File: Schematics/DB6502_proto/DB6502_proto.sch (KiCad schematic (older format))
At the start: 28 parts, among them SW1 Reset, U1 DS1813, U10 62256, U11 74AC138, U12 28C256, U13 22V10C, U2 74AC32, U3 74HC21, U4 65C02S, U5 74AC74, U6 74HC74, U7 74AC04, U8 62256, U9 74AC08, X1 14MHz

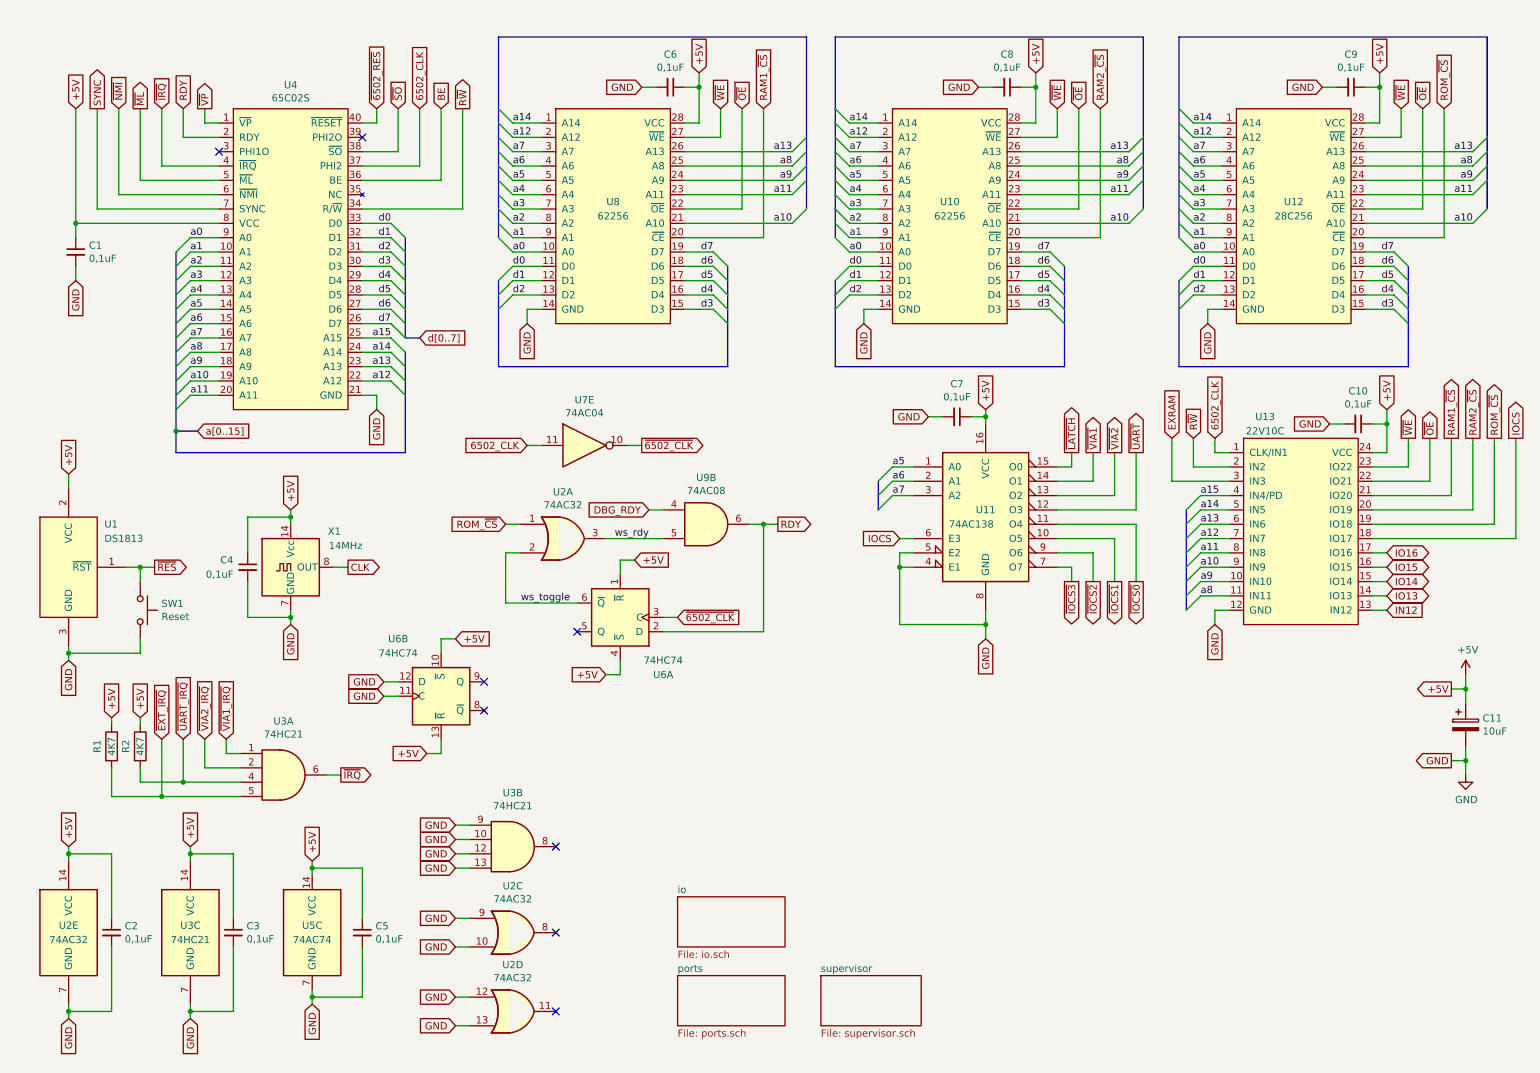
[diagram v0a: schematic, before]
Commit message: Added second USB channel to UART
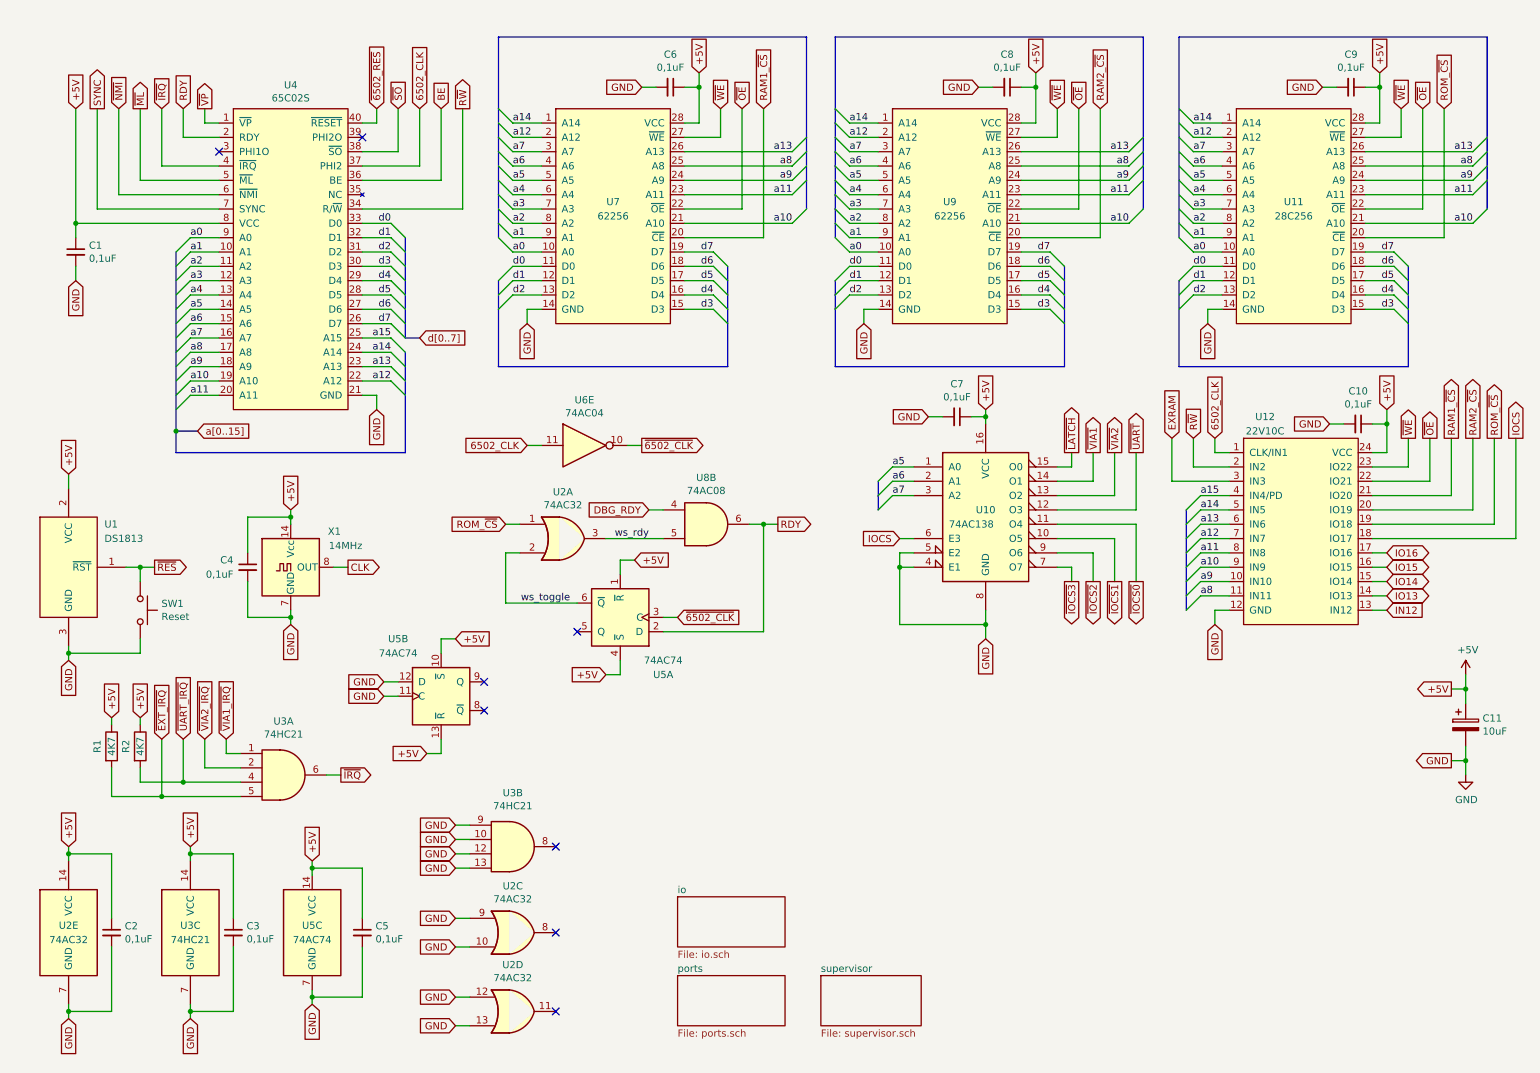
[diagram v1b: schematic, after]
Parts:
- C1, C10, C2, C3, C4, C5, C6, C7, C8, C9: footprint (none) -> Capacitor_THT:C_Disc_D5.0mm_W2.5mm_P2.50mm
- R1, R2: footprint (none) -> Resistor_THT:R_Axial_DIN0207_L6.3mm_D2.5mm_P10.16mm_Horizontal
- U2, U5: footprint (none) -> Package_DIP:DIP-14_W7.62mm_Socket
- U3: footprint (none) -> Package_DIP:DIP-12_W7.62mm_Socket
- U5: renamed from U6; value 74HC74 -> 74AC74; footprint (none) -> Package_DIP:DIP-14_W7.62mm_Socket
- U6: renamed from U7; footprint (none) -> Package_DIP:DIP-14_W7.62mm_Socket
- U8: renamed from U9; footprint (none) -> Package_DIP:DIP-14_W7.62mm_Socket
- renumbered U11 to U10, U12 to U11, U13 to U12, U8 to U7, U10 to U9
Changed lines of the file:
@@
 	10600 5200 10600 5300
 $Comp
-L 6502:22V10C U13
+L 6502:22V10C U12
 U 1 1 5F680A6E
 P 9450 4100
-F 0 "U13" H 9200 4900 50  0000 C CNN
+F 0 "U12" H 9200 4900 50  0000 C CNN
 F 1 "22V10C" H 9200 4800 50  0000 C CNN
 F 2 "Package_DIP:DIP-24_W7.62mm_Socket" H 9450 3400 50  0001 C CNN
@@
 Connection ~ 1350 4350
 $Comp
-L 74xx:74LS138 U11
+L 74xx:74LS138 U10
 U 1 1 5F9A1F2C
 P 7250 3950
-F 0 "U11" H 7250 3950 50  0000 C CNN
+F 0 "U10" H 7250 3950 50  0000 C CNN
 F 1 "74AC138" H 7150 3850 50  0000 C CNN
 F 2 "Package_DIP:DIP-16_W7.62mm_Socket" H 7250 3950 50  0001 C CNN
@@
 $EndComp
 $Comp
-L 6502:62256 U10
+L 6502:62256 U9
 U 1 1 5F5FD943
 P 7000 1900
-F 0 "U10" H 7000 2000 50  0000 C CNN
+F 0 "U9" H 7000 2000 50  0000 C CNN
 F 1 "62256" H 7000 1900 50  0000 C CNN
 F 2 "Package_DIP:DIP-28_W15.24mm_Socket" H 6950 2700 50  0001 C CNN
@@
 $EndComp
 $Comp
-L 6502:62256 U8
+L 6502:62256 U7
 U 1 1 5F5BE432
 P 4650 1900
-F 0 "U8" H 4650 2000 50  0000 C CNN
+F 0 "U7" H 4650 2000 50  0000 C CNN
 F 1 "62256" H 4650 1900 50  0000 C CNN
 F 2 "Package_DIP:DIP-28_W15.24mm_Socket" H 4600 2700 50  0001 C CNN
@@
 $EndComp
 $Comp
-L 6502:28C256 U12
+L 6502:28C256 U11
 U 1 1 5F605CEF
 P 9400 1900
-F 0 "U12" H 9400 2000 50  0000 C CNN
+F 0 "U11" H 9400 2000 50  0000 C CNN
 F 1 "28C256" H 9400 1900 50  0000 C CNN
 F 2 "Package_DIP:DIP-28_W15.24mm_Socket" H 9350 2700 50  0001 C CNN
@@
 P 4450 3500
 AR Path="/5F8F4E1E/5FD6D1DD" Ref="U?"  Part="5"
-AR Path="/5FD6D1DD" Ref="U7"  Part="5"
-F 0 "U7" H 4450 3817 50  0000 C CNN
+AR Path="/5FD6D1DD" Ref="U6"  Part="5"
+F 0 "U6" H 4450 3817 50  0000 C CNN
 F 1 "74AC04" H 4450 3726 50  0000 C CNN
-F 2 "" H 4450 3500 50  0001 C CNN
+F 2 "Package_DIP:DIP-14_W7.62mm_Socket" H 4450 3500 50  0001 C CNN
 F 3 "https://www.ti.com/lit/ds/symlink/sn74ac04.pdf" H 4450 3500 50  0001 C CNN
 	5    4450 3500
@@
 P 5300 4050
 AR Path="/5F8F4E1E/5FDA6F78" Ref="U?"  Part="2"
-AR Path="/5FDA6F78" Ref="U9"  Part="2"
-F 0 "U9" H 5300 4375 50  0000 C CNN
+AR Path="/5FDA6F78" Ref="U8"  Part="2"
+F 0 "U8" H 5300 4375 50  0000 C CNN
 F 1 "74AC08" H 5300 4284 50  0000 C CNN
-F 2 "" H 5300 4050 50  0001 C CNN
+F 2 "Package_DIP:DIP-14_W7.62mm_Socket" H 5300 4050 50  0001 C CNN
 F 3 "https://www.ti.com/lit/ds/symlink/sn74ac08.pdf" H 5300 4050 50  0001 C CNN
 	2    5300 4050
@@
 F 0 "U2" H 4300 4475 50  0000 C CNN
 F 1 "74AC32" H 4300 4384 50  0000 C CNN
-F 2 "" H 4300 4150 50  0001 C CNN
+F 2 "Package_DIP:DIP-14_W7.62mm_Socket" H 4300 4150 50  0001 C CNN
 F 3 "http://www.ti.com/lit/gpn/sn74LS32" H 4300 4150 50  0001 C CNN
 	1    4300 4150
@@
 P 4700 4700
 AR Path="/5F8F4E1E/5FE3D22B" Ref="U?"  Part="2"
-AR Path="/5FE3D22B" Ref="U6"  Part="1"
-F 0 "U6" H 4400 5100 50  0000 C CNN
-F 1 "74HC74" H 4400 5000 50  0000 C CNN
-F 2 "" H 4700 4700 50  0001 C CNN
+AR Path="/5FE3D22B" Ref="U5"  Part="1"
+F 0 "U5" H 4400 5100 50  0000 C CNN
+F 1 "74AC74" H 4400 5000 50  0000 C CNN
+F 2 "Package_DIP:DIP-14_W7.62mm_Socket" H 4700 4700 50  0001 C CNN
 F 3 "74xx/74hc_hct74.pdf" H 4700 4700 50  0001 C CNN
 	1    4700 4700
@@
 F 0 "C1" H 992 2196 50  0000 L CNN
 F 1 "0,1uF" H 992 2105 50  0000 L CNN
-F 2 "" H 900 2150 50  0001 C CNN
+F 2 "Capacitor_THT:C_Disc_D5.0mm_W2.5mm_P2.50mm" H 900 2150 50  0001 C CNN
 F 3 "~" H 900 2150 50  0001 C CNN
 	1    900  2150
@@
 F 0 "C6" V 4821 1000 50  0000 C CNN
 F 1 "0,1uF" V 4912 1000 50  0000 C CNN
-F 2 "" H 5050 1000 50  0001 C CNN
+F 2 "Capacitor_THT:C_Disc_D5.0mm_W2.5mm_P2.50mm" H 5050 1000 50  0001 C CNN
 F 3 "~" H 5050 1000 50  0001 C CNN
 	1    5050 1000
@@
 F 0 "C8" V 7171 1000 50  0000 C CNN
 F 1 "0,1uF" V 7262 1000 50  0000 C CNN
-F 2 "" H 7400 1000 50  0001 C CNN
+F 2 "Capacitor_THT:C_Disc_D5.0mm_W2.5mm_P2.50mm" H 7400 1000 50  0001 C CNN
 F 3 "~" H 7400 1000 50  0001 C CNN
 	1    7400 1000
@@
 F 0 "C9" V 9571 1000 50  0000 C CNN
 F 1 "0,1uF" V 9662 1000 50  0000 C CNN
-F 2 "" H 9800 1000 50  0001 C CNN
+F 2 "Capacitor_THT:C_Disc_D5.0mm_W2.5mm_P2.50mm" H 9800 1000 50  0001 C CNN
 F 3 "~" H 9800 1000 50  0001 C CNN
 	1    9800 1000
@@
 F 0 "C10" V 9621 3350 50  0000 C CNN
 F 1 "0,1uF" V 9712 3350 50  0000 C CNN
-F 2 "" H 9850 3350 50  0001 C CNN
+F 2 "Capacitor_THT:C_Disc_D5.0mm_W2.5mm_P2.50mm" H 9850 3350 50  0001 C CNN
 F 3 "~" H 9850 3350 50  0001 C CNN
 	1    9850 3350
@@
 F 0 "C7" V 6821 3300 50  0000 C CNN
 F 1 "0,1uF" V 6912 3300 50  0000 C CNN
-F 2 "" H 7050 3300 50  0001 C CNN
+F 2 "Capacitor_THT:C_Disc_D5.0mm_W2.5mm_P2.50mm" H 7050 3300 50  0001 C CNN
 F 3 "~" H 7050 3300 50  0001 C CNN
 	1    7050 3300
@@
 F 0 "C4" H 2000 4400 50  0000 R CNN
 F 1 "0,1uF" H 2000 4300 50  0000 R CNN
-F 2 "" H 2100 4350 50  0001 C CNN
+F 2 "Capacitor_THT:C_Disc_D5.0mm_W2.5mm_P2.50mm" H 2100 4350 50  0001 C CNN
 F 3 "~" H 2100 4350 50  0001 C CNN
 	1    2100 4350
@@
 F 0 "U2" H 850 6950 50  0000 C CNN
 F 1 "74AC32" H 850 6850 50  0000 C CNN
-F 2 "" H 850 6900 50  0001 C CNN
+F 2 "Package_DIP:DIP-14_W7.62mm_Socket" H 850 6900 50  0001 C CNN
 F 3 "http://www.ti.com/lit/gpn/sn74LS32" H 850 6900 50  0001 C CNN
 	5    850  6900
@@
 F 0 "C2" H 1242 6946 50  0000 L CNN
 F 1 "0,1uF" H 1242 6855 50  0000 L CNN
-F 2 "" H 1150 6900 50  0001 C CNN
+F 2 "Capacitor_THT:C_Disc_D5.0mm_W2.5mm_P2.50mm" H 1150 6900 50  0001 C CNN
 F 3 "~" H 1150 6900 50  0001 C CNN
 	1    1150 6900
@@
 F 0 "U2" H 3950 7225 50  0000 C CNN
 F 1 "74AC32" H 3950 7134 50  0000 C CNN
-F 2 "" H 3950 6900 50  0001 C CNN
+F 2 "Package_DIP:DIP-14_W7.62mm_Socket" H 3950 6900 50  0001 C CNN
 F 3 "http://www.ti.com/lit/gpn/sn74LS32" H 3950 6900 50  0001 C CNN
 	3    3950 6900
@@
 F 0 "U2" H 3950 7775 50  0000 C CNN
 F 1 "74AC32" H 3950 7684 50  0000 C CNN
-F 2 "" H 3950 7450 50  0001 C CNN
+F 2 "Package_DIP:DIP-14_W7.62mm_Socket" H 3950 7450 50  0001 C CNN
 F 3 "http://www.ti.com/lit/gpn/sn74LS32" H 3950 7450 50  0001 C CNN
 	4    3950 7450
@@
 F 0 "U3" H 2350 6175 50  0000 C CNN
 F 1 "74HC21" H 2350 6084 50  0000 C CNN
-F 2 "" H 2350 5800 50  0001 C CNN
+F 2 "Package_DIP:DIP-12_W7.62mm_Socket" H 2350 5800 50  0001 C CNN
 F 3 "http://www.ti.com/lit/gpn/sn74LS21" H 2350 5800 50  0001 C CNN
 	1    2350 5800
@@
 F 0 "U3" H 3950 6675 50  0000 C CNN
 F 1 "74HC21" H 3950 6584 50  0000 C CNN
-F 2 "" H 3950 6300 50  0001 C CNN
+F 2 "Package_DIP:DIP-12_W7.62mm_Socket" H 3950 6300 50  0001 C CNN
 F 3 "http://www.ti.com/lit/gpn/sn74LS21" H 3950 6300 50  0001 C CNN
 	2    3950 6300
@@
 F 0 "U3" H 1700 6950 50  0000 C CNN
 F 1 "74HC21" H 1700 6850 50  0000 C CNN
-F 2 "" H 1700 6900 50  0001 C CNN
+F 2 "Package_DIP:DIP-12_W7.62mm_Socket" H 1700 6900 50  0001 C CNN
 F 3 "http://www.ti.com/lit/gpn/sn74LS21" H 1700 6900 50  0001 C CNN
 	3    1700 6900
@@
 F 0 "C3" H 2092 6946 50  0000 L CNN
 F 1 "0,1uF" H 2092 6855 50  0000 L CNN
-F 2 "" H 2000 6900 50  0001 C CNN
+F 2 "Capacitor_THT:C_Disc_D5.0mm_W2.5mm_P2.50mm" H 2000 6900 50  0001 C CNN
 F 3 "~" H 2000 6900 50  0001 C CNN
 	1    2000 6900
@@
 F 0 "R1" V 1050 5600 50  0000 C CNN
 F 1 "4K7" V 1150 5600 50  0000 C CNN
-F 2 "" V 1080 5600 50  0001 C CNN
+F 2 "Resistor_THT:R_Axial_DIN0207_L6.3mm_D2.5mm_P10.16mm_Horizontal" V 1080 5600 50  0001 C CNN
 F 3 "~" H 1150 5600 50  0001 C CNN
 	1    1150 5600
@@
 F 0 "U5" H 2550 6950 50  0000 C CNN
 F 1 "74AC74" H 2550 6850 50  0000 C CNN
-F 2 "" H 2550 6900 50  0001 C CNN
+F 2 "Package_DIP:DIP-14_W7.62mm_Socket" H 2550 6900 50  0001 C CNN
 F 3 "74xx/74hc_hct74.pdf" H 2550 6900 50  0001 C CNN
 	3    2550 6900
@@
 F 0 "C5" H 2992 6946 50  0000 L CNN
 F 1 "0,1uF" H 2992 6855 50  0000 L CNN
-F 2 "" H 2900 6900 50  0001 C CNN
+F 2 "Capacitor_THT:C_Disc_D5.0mm_W2.5mm_P2.50mm" H 2900 6900 50  0001 C CNN
 F 3 "~" H 2900 6900 50  0001 C CNN
 	1    2900 6900
@@
 P 3450 5250
 AR Path="/5F8F4E1E/5FE82338" Ref="U?"  Part="2"
-AR Path="/5FE82338" Ref="U6"  Part="2"
-F 0 "U6" H 3150 5650 50  0000 C CNN
-F 1 "74HC74" H 3150 5550 50  0000 C CNN
-F 2 "" H 3450 5250 50  0001 C CNN
+AR Path="/5FE82338" Ref="U5"  Part="2"
+F 0 "U5" H 3150 5650 50  0000 C CNN
+F 1 "74AC74" H 3150 5550 50  0000 C CNN
+F 2 "Package_DIP:DIP-14_W7.62mm_Socket" H 3450 5250 50  0001 C CNN
 F 3 "74xx/74hc_hct74.pdf" H 3450 5250 50  0001 C CNN
 	2    3450 5250
@@
 F 0 "R2" V 1250 5600 50  0000 C CNN
 F 1 "4K7" V 1350 5600 50  0000 C CNN
-F 2 "" V 1280 5600 50  0001 C CNN
+F 2 "Resistor_THT:R_Axial_DIN0207_L6.3mm_D2.5mm_P10.16mm_Horizontal" V 1280 5600 50  0001 C CNN
 F 3 "~" H 1350 5600 50  0001 C CNN
 	1    1350 5600

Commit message: Massive cleanup of the schematic
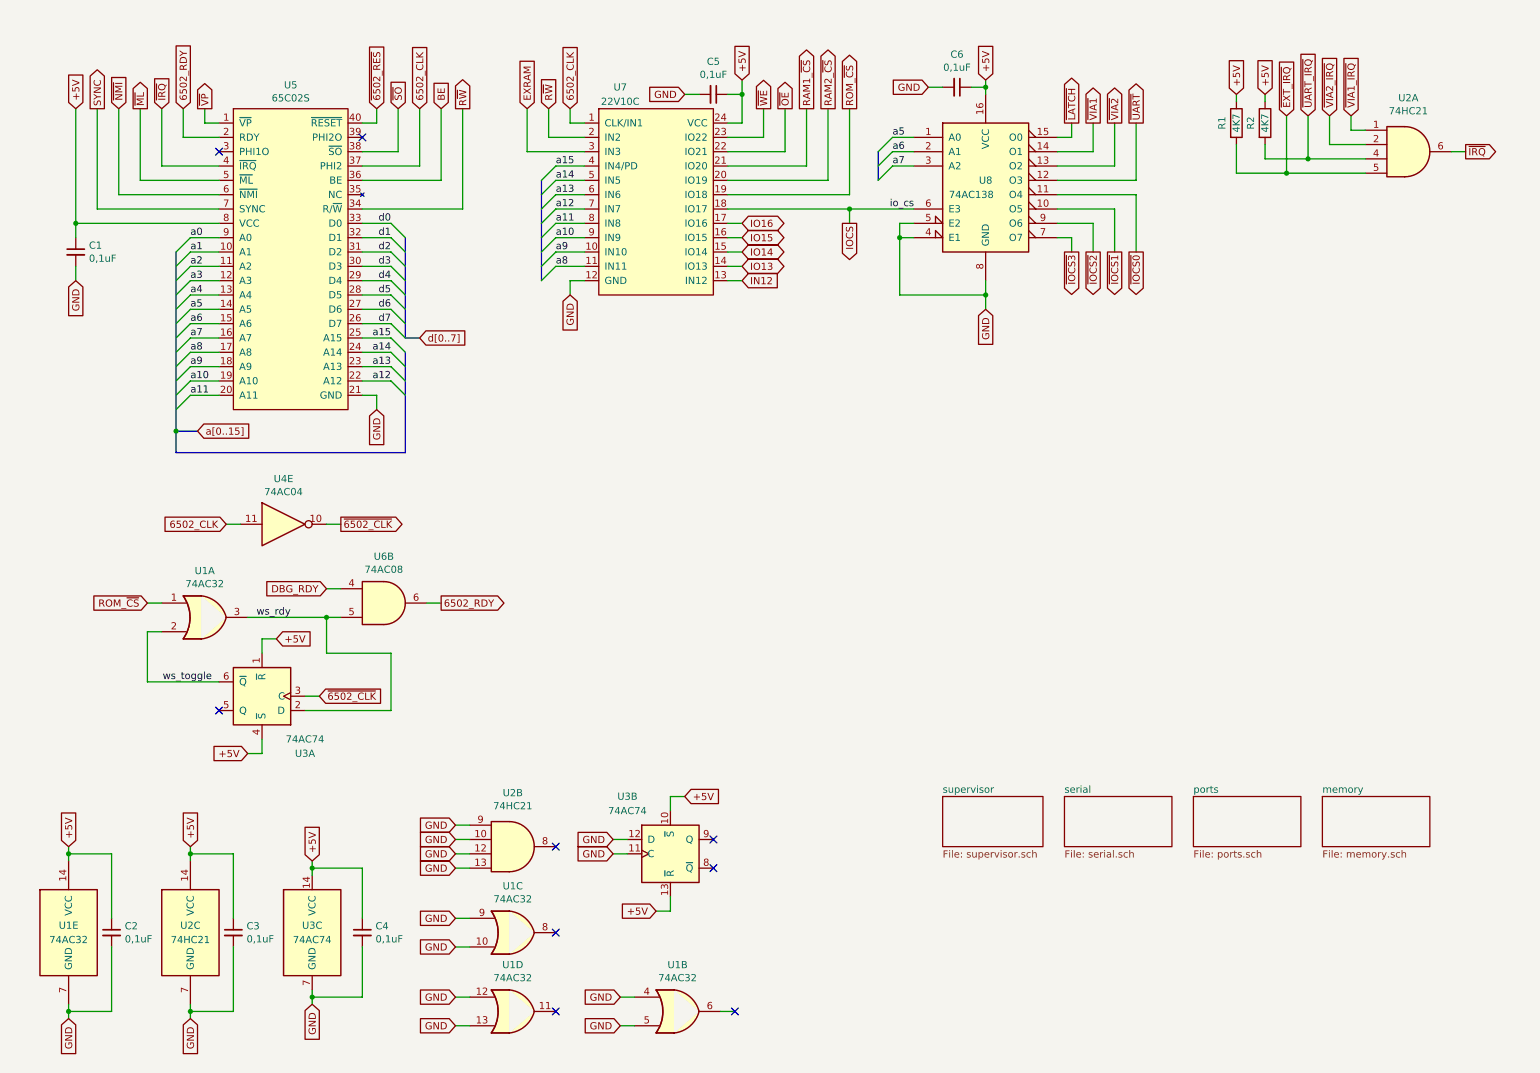
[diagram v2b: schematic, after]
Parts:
- removed C11: 10uF, Capacitor_THT:CP_Radial_D4.0mm_P2.00mm, symbol Device:CP
- removed C4, C6, C8, C9: 0,1uF, Capacitor_THT:C_Disc_D5.0mm_W2.5mm_P2.50mm, symbol Device:C_Small
- removed SW1: Reset, Button_Switch_THT:SW_PUSH_6mm_H4.3mm, symbol Switch:SW_Push
- removed U1: DS1813, Package_TO_SOT_THT:TO-92_Inline_Wide, symbol 6502:DS1813
- removed U11: 28C256, Package_DIP:DIP-28_W15.24mm_Socket, symbol 6502:28C256
- removed U7, U9: 62256, Package_DIP:DIP-28_W15.24mm_Socket, symbol 6502:62256
- removed X1: 14MHz, Oscillator:Oscillator_DIP-14, symbol Oscillator:ACO-xxxMHz
- added unit 2 of U1
- renumbered C5 to C4, C10 to C5, C7 to C6, U2 to U1, U3 to U2, U5 to U3, U6 to U4, U4 to U5, U8 to U6, U12 to U7, U10 to U8
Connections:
- net GND: now also U1.4, U1.5
- net ws_rdy: now also U3.2 (D)
- net RDY renamed 6502_RDY
- net 6502_RDY: no longer U3.2 (D)
- no-connect marks 8 -> 9
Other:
- moved on the sheet: C5, C6, R1, R2, U1A, U2A, U3A, U3B, U4E, U6B, U7, U8
